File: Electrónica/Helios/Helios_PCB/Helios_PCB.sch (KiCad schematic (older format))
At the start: 10 parts, among them U0 OPA2380, U1 OPA2380

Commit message: Helios -Sch Update
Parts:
- F0, F1, F2, F3: footprint (none) -> Helios:SFH2704_Photodiode
- U0, U1: footprint (none) -> Helios:OPA2380
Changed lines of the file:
@@
 F 0 "F3" V 5150 6078 50  0000 L CNN
 F 1 "SFH2704" H 5150 6124 50  0001 C CNN
-F 2 "" H 5150 5650 50  0001 C CNN
-F 3 "" H 5150 5650 50  0001 C CNN
+F 2 "Helios:SFH2704_Photodiode" H 5150 5650 50  0001 C CNN
+F 3 "2704_Photodiode.pdf" H 5150 5650 50  0001 C CNN
 	1    5150 5650
 	0    1    1    0
@@
 F 0 "U1" H 4150 5515 50  0000 C CNN
 F 1 "OPA2380" H 4150 5424 50  0000 C CNN
-F 2 "" H 4150 5100 50  0001 C CNN
-F 3 "" H 4150 5100 50  0001 C CNN
+F 2 "Helios:OPA2380" H 4150 5100 50  0001 C CNN
+F 3 "$(KICAD_DATASHEET_DIR)/opa2380.pdf" H 4150 5100 50  0001 C CNN
 	1    4150 5100
 	1    0    0    -1
@@
 	3800 5250 3650 5250
 $Comp
-L power:VCC #PWR?
+L power:VCC #PWR0101
 U 1 1 62E0D333
 P 4650 4800
-F 0 "#PWR?" H 4650 4650 50  0001 C CNN
+F 0 "#PWR0101" H 4650 4650 50  0001 C CNN
 F 1 "VCC" H 4665 4973 50  0000 C CNN
 F 2 "" H 4650 4800 50  0001 C CNN
@@
 	3650 5250 3650 5400
 $Comp
-L power:GND #PWR?
+L power:GND #PWR0102
 U 1 1 62E0BF47
 P 3650 5400
-F 0 "#PWR?" H 3650 5150 50  0001 C CNN
+F 0 "#PWR0102" H 3650 5150 50  0001 C CNN
 F 1 "GND" H 3655 5227 50  0000 C CNN
 F 2 "" H 3650 5400 50  0001 C CNN
@@
 $EndComp
 $Comp
-L power:GND #PWR?
+L power:GND #PWR0103
 U 1 1 62E116A7
 P 4650 5400
-F 0 "#PWR?" H 4650 5150 50  0001 C CNN
+F 0 "#PWR0103" H 4650 5150 50  0001 C CNN
 F 1 "GND" H 4655 5227 50  0000 C CNN
 F 2 "" H 4650 5400 50  0001 C CNN
@@
 	4650 5250 4500 5250
 $Comp
-L power:GND #PWR?
+L power:GND #PWR0104
 U 1 1 62E11BF6
 P 5150 6150
-F 0 "#PWR?" H 5150 5900 50  0001 C CNN
+F 0 "#PWR0104" H 5150 5900 50  0001 C CNN
 F 1 "GND" H 5155 5977 50  0000 C CNN
 F 2 "" H 5150 6150 50  0001 C CNN
@@
 Connection ~ 3650 5250
 $Comp
-L power:GND #PWR?
+L power:GND #PWR0105
 U 1 1 62E13C31
 P 3150 6150
-F 0 "#PWR?" H 3150 5900 50  0001 C CNN
+F 0 "#PWR0105" H 3150 5900 50  0001 C CNN
 F 1 "GND" H 3155 5977 50  0000 C CNN
 F 2 "" H 3150 6150 50  0001 C CNN
@@
 F 0 "F2" V 3150 6078 50  0000 L CNN
 F 1 "SFH2704" H 3150 6124 50  0001 C CNN
-F 2 "" H 3150 5650 50  0001 C CNN
-F 3 "" H 3150 5650 50  0001 C CNN
+F 2 "Helios:SFH2704_Photodiode" H 3150 5650 50  0001 C CNN
+F 3 "2704_Photodiode.pdf" H 3150 5650 50  0001 C CNN
 	1    3150 5650
 	0    1    1    0
@@
 F 0 "F1" V 5150 3078 50  0000 L CNN
 F 1 "SFH2704" H 5150 3124 50  0001 C CNN
-F 2 "" H 5150 2650 50  0001 C CNN
-F 3 "" H 5150 2650 50  0001 C CNN
+F 2 "Helios:SFH2704_Photodiode" H 5150 2650 50  0001 C CNN
+F 3 "$(KICAD_DATASHEET_DIR)/SFH 2704_Photodiode.pdf" H 5150 2650 50  0001 C CNN
 	1    5150 2650
 	0    1    1    0
@@
 F 0 "U0" H 4150 2515 50  0000 C CNN
 F 1 "OPA2380" H 4150 2424 50  0000 C CNN
-F 2 "" H 4150 2100 50  0001 C CNN
-F 3 "" H 4150 2100 50  0001 C CNN
+F 2 "Helios:OPA2380" H 4150 2100 50  0001 C CNN
+F 3 "$(KICAD_DATASHEET_DIR)/opa2380.pdf" H 4150 2100 50  0001 C CNN
 	1    4150 2100
 	1    0    0    -1
@@
 	3800 2250 3650 2250
 $Comp
-L power:VCC #PWR?
+L power:VCC #PWR0106
 U 1 1 62E1E0EE
 P 4650 1800
-F 0 "#PWR?" H 4650 1650 50  0001 C CNN
+F 0 "#PWR0106" H 4650 1650 50  0001 C CNN
 F 1 "VCC" H 4665 1973 50  0000 C CNN
 F 2 "" H 4650 1800 50  0001 C CNN
@@
 	3650 2250 3650 2400
 $Comp
-L power:GND #PWR?
+L power:GND #PWR0107
 U 1 1 62E1E0F9
 P 3650 2400
-F 0 "#PWR?" H 3650 2150 50  0001 C CNN
+F 0 "#PWR0107" H 3650 2150 50  0001 C CNN
 F 1 "GND" H 3655 2227 50  0000 C CNN
 F 2 "" H 3650 2400 50  0001 C CNN
@@
 $EndComp
 $Comp
-L power:GND #PWR?
+L power:GND #PWR0108
 U 1 1 62E1E0FF
 P 4650 2400
-F 0 "#PWR?" H 4650 2150 50  0001 C CNN
+F 0 "#PWR0108" H 4650 2150 50  0001 C CNN
 F 1 "GND" H 4655 2227 50  0000 C CNN
 F 2 "" H 4650 2400 50  0001 C CNN
@@
 	4650 2250 4500 2250
 $Comp
-L power:GND #PWR?
+L power:GND #PWR0109
 U 1 1 62E1E107
 P 5150 3150
-F 0 "#PWR?" H 5150 2900 50  0001 C CNN
+F 0 "#PWR0109" H 5150 2900 50  0001 C CNN
 F 1 "GND" H 5155 2977 50  0000 C CNN
 F 2 "" H 5150 3150 50  0001 C CNN
@@
 Connection ~ 3650 2250
 $Comp
-L power:GND #PWR?
+L power:GND #PWR0110
 U 1 1 62E1E113
 P 3150 3150
-F 0 "#PWR?" H 3150 2900 50  0001 C CNN
+F 0 "#PWR0110" H 3150 2900 50  0001 C CNN
 F 1 "GND" H 3155 2977 50  0000 C CNN
 F 2 "" H 3150 3150 50  0001 C CNN
@@
 F 0 "F0" V 3150 3078 50  0000 L CNN
 F 1 "SFH2704" H 3150 3124 50  0001 C CNN
-F 2 "" H 3150 2650 50  0001 C CNN
-F 3 "" H 3150 2650 50  0001 C CNN
+F 2 "Helios:SFH2704_Photodiode" H 3150 2650 50  0001 C CNN
+F 3 "2704_Photodiode.pdf" H 3150 2650 50  0001 C CNN
 	1    3150 2650
 	0    1    1    0

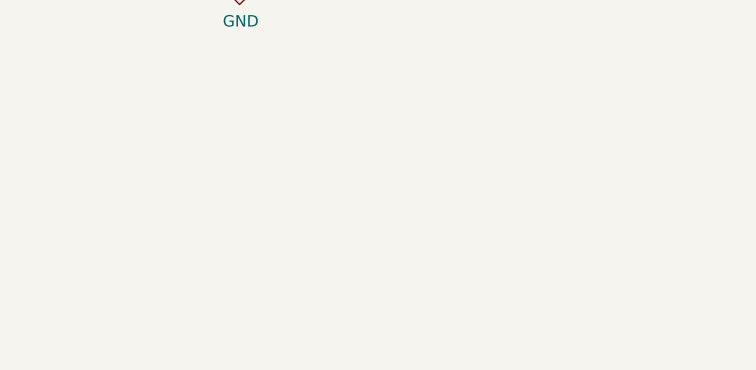
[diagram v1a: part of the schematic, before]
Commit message: Helios -  Added Connectors
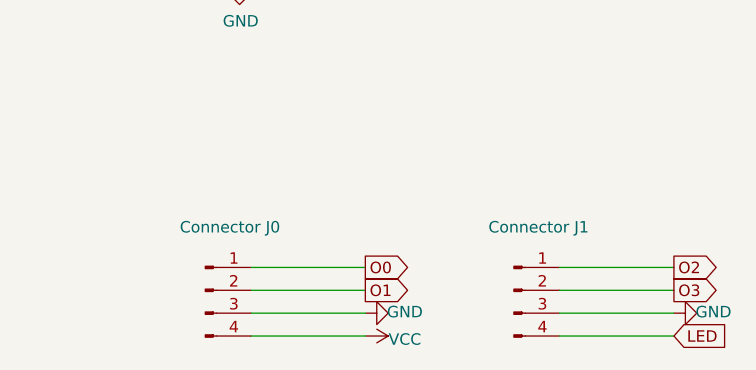
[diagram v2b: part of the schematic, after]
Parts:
- added J0: Connector J0, Connector_PinHeader_2.00mm:PinHeader_1x04_P2.00mm_Vertical, symbol Connector:Conn_01x04_Male
- added J1: Connector J1, Connector_PinHeader_2.00mm:PinHeader_1x04_P2.00mm_Vertical, symbol Connector:Conn_01x04_Male
- R0, R1, R2, R3: footprint (none) -> Helios:RS_0805
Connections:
- net GND: now also J0.3 (Pin_3), J1.3 (Pin_3)
- net O0: now also J0.1 (Pin_1)
- net O1: now also J0.2 (Pin_2)
- net O2: now also J1.1 (Pin_1)
- net O3: now also J1.2 (Pin_2)
- net VCC: now also J0.4 (Pin_4)
- new net LED: J1.4 (Pin_4)
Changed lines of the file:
@@
 F 0 "R2" H 3220 4846 50  0001 L CNN
 F 1 "R" H 3220 4800 50  0000 L CNN
-F 2 "" V 3080 4800 50  0001 C CNN
-F 3 "~" H 3150 4800 50  0001 C CNN
+F 2 "Helios:RS_0805" V 3080 4800 50  0001 C CNN
+F 3 "$(KICAD_DATASHEET_DIR)/2M2_Resistance.pdf" H 3150 4800 50  0001 C CNN
 	1    3150 4800
 	1    0    0    -1
@@
 F 0 "R3" H 5220 4846 50  0001 L CNN
 F 1 "R" H 5220 4800 50  0000 L CNN
-F 2 "" V 5080 4800 50  0001 C CNN
-F 3 "~" H 5150 4800 50  0001 C CNN
+F 2 "Helios:RS_0805" V 5080 4800 50  0001 C CNN
+F 3 "$(KICAD_DATASHEET_DIR)/2M2_Resistance.pdf" H 5150 4800 50  0001 C CNN
 	1    5150 4800
 	1    0    0    -1
@@
 F 0 "R0" H 3220 1846 50  0001 L CNN
 F 1 "R" H 3220 1800 50  0000 L CNN
-F 2 "" V 3080 1800 50  0001 C CNN
-F 3 "~" H 3150 1800 50  0001 C CNN
+F 2 "Helios:RS_0805" V 3080 1800 50  0001 C CNN
+F 3 "$(KICAD_DATASHEET_DIR)/2M2_Resistance.pdf" H 3150 1800 50  0001 C CNN
 	1    3150 1800
 	1    0    0    -1
@@
 F 0 "R1" H 5220 1846 50  0001 L CNN
 F 1 "R" H 5220 1800 50  0000 L CNN
-F 2 "" V 5080 1800 50  0001 C CNN
-F 3 "~" H 5150 1800 50  0001 C CNN
+F 2 "Helios:RS_0805" V 5080 1800 50  0001 C CNN
+F 3 "$(KICAD_DATASHEET_DIR)/2M2_Resistance.pdf" H 5150 1800 50  0001 C CNN
 	1    5150 1800
 	1    0    0    -1
@@
 EndData
 $EndBitmap
+Text GLabel 5700 7400 2    50   Output ~ 0
+O0
+Wire Wire Line
+	5700 7400 5200 7400
+Text GLabel 5700 7500 2    50   Output ~ 0
+O1
+Wire Wire Line
+	5700 7500 5200 7500
+Wire Wire Line
+	5700 7600 5200 7600
+Wire Wire Line
+	5700 7700 5200 7700
+$Comp
+L Connector:Conn_01x04_Male J0
+U 1 1 62E043F9
+P 5000 7500
+F 0 "J0" H 5108 7781 50  0001 C CNN
+F 1 "Connector J0" H 5108 7776 50  0000 C CNN
+F 2 "Connector_PinHeader_2.00mm:PinHeader_1x04_P2.00mm_Vertical" H 5000 7500 50  0001 C CNN
+F 3 "~" H 5000 7500 50  0001 C CNN
+	1    5000 7500
+	1    0    0    -1
+$EndComp
+$Comp
+L power:GND #PWR?
+U 1 1 62E1157C
+P 5700 7600
+F 0 "#PWR?" H 5700 7350 50  0001 C CNN
+F 1 "GND" V 5705 7427 50  0000 C CNN
+F 2 "" H 5700 7600 50  0001 C CNN
+F 3 "" H 5700 7600 50  0001 C CNN
+	1    5700 7600
+	0    -1   -1   0
+$EndComp
+$Comp
+L power:VCC #PWR?
+U 1 1 62E1494B
+P 5700 7700
+F 0 "#PWR?" H 5700 7550 50  0001 C CNN
+F 1 "VCC" V 5715 7873 50  0000 C CNN
+F 2 "" H 5700 7700 50  0001 C CNN
+F 3 "" H 5700 7700 50  0001 C CNN
+	1    5700 7700
+	0    1    1    0
+$EndComp
+Text GLabel 7050 7400 2    50   Output ~ 0
+O2
+Wire Wire Line
+	7050 7400 6550 7400
+Text GLabel 7050 7500 2    50   Output ~ 0
+O3
+Wire Wire Line
+	7050 7500 6550 7500
+Wire Wire Line
+	7050 7600 6550 7600
+$Comp
+L Connector:Conn_01x04_Male J1
+U 1 1 62E18AA8
+P 6350 7500
+F 0 "J1" H 6458 7781 50  0001 C CNN
+F 1 "Connector J1" H 6458 7776 50  0000 C CNN
+F 2 "Connector_PinHeader_2.00mm:PinHeader_1x04_P2.00mm_Vertical" H 6350 7500 50  0001 C CNN
+F 3 "~" H 6350 7500 50  0001 C CNN
+	1    6350 7500
+	1    0    0    -1
+$EndComp
+$Comp
+L power:GND #PWR?
+U 1 1 62E18AAE
+P 7050 7600
+F 0 "#PWR?" H 7050 7350 50  0001 C CNN
+F 1 "GND" V 7055 7427 50  0000 C CNN
+F 2 "" H 7050 7600 50  0001 C CNN
+F 3 "" H 7050 7600 50  0001 C CNN
+	1    7050 7600
+	0    -1   -1   0
+$EndComp
+Text GLabel 7050 7700 2    50   Input ~ 0
+LED
+Wire Wire Line
+	7050 7700 6550 7700
 $EndSCHEMATC

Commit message: Helios: VCC routing
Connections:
- net O0: now also R1.1, U0.7 (OB); no longer R0.1, U0.1 (OA)
- net O1: now also R0.1, U0.1 (OA); no longer R1.1, U0.7 (OB)
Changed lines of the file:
@@
 $EndComp
 Text GLabel 2650 1500 0    50   Output ~ 0
-O0
+O1
 Wire Wire Line
 	2650 1500 3150 1500
 Connection ~ 3150 1500
 Text GLabel 5650 1500 2    50   Output ~ 0
-O1
+O0
 Wire Wire Line
 	5650 1500 5150 1500
@@
 $EndComp
 $Comp
-L power:GND #PWR?
+L power:GND #PWR0111
 U 1 1 62E1157C
 P 5700 7600
-F 0 "#PWR?" H 5700 7350 50  0001 C CNN
+F 0 "#PWR0111" H 5700 7350 50  0001 C CNN
 F 1 "GND" V 5705 7427 50  0000 C CNN
 F 2 "" H 5700 7600 50  0001 C CNN
@@
 $EndComp
 $Comp
-L power:VCC #PWR?
+L power:VCC #PWR0112
 U 1 1 62E1494B
 P 5700 7700
-F 0 "#PWR?" H 5700 7550 50  0001 C CNN
+F 0 "#PWR0112" H 5700 7550 50  0001 C CNN
 F 1 "VCC" V 5715 7873 50  0000 C CNN
 F 2 "" H 5700 7700 50  0001 C CNN
@@
 $EndComp
 $Comp
-L power:GND #PWR?
+L power:GND #PWR0113
 U 1 1 62E18AAE
 P 7050 7600
-F 0 "#PWR?" H 7050 7350 50  0001 C CNN
+F 0 "#PWR0113" H 7050 7350 50  0001 C CNN
 F 1 "GND" V 7055 7427 50  0000 C CNN
 F 2 "" H 7050 7600 50  0001 C CNN
